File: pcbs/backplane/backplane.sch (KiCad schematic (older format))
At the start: 6 parts, among them P1 CONN_02X04, P2 CONN_02X04, P3 USB_B, P4 CONN_02X09, P5 CONN_02X09, U1 FT232RL

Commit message: Updated electrical spec.
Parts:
- removed P1, P2: CONN_02X04, Pin_Headers:Pin_Header_Straight_2x04, symbol CONN_02X04
- removed P4, P5: CONN_02X09, Pin_Headers:Pin_Header_Straight_2x09, symbol CONN_02X09
- removed U1: FT232RL, Housings_SSOP:SSOP-28_5.3x10.2mm_Pitch0.65mm, symbol FT232RL
- added P1, P2: CONN_02X03, Pin_Headers:Pin_Header_Straight_2x03, symbol CONN_02X03
- added P4, P5: CONN_02X07, Pin_Headers:Pin_Header_Straight_2x07, symbol CONN_02X07
- added U1: CH340G, SMD_Packages:SO-16-N, symbol CH340G
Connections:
- net labels added: 5V, ADC4, GPIO0, UART_RX, nRST
- net labels removed: PWM1, PWM2, SPI_CLK, SPI_CS, SPI_MISO, SPI_MOSI, VCC, Vcc
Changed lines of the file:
@@
 LIBS:silabs
 LIBS:ft232rl
+LIBS:ch340g
 LIBS:backplane-cache
 EELAYER 25 0
@@
 $EndDescr
 $Comp
-L CONN_02X04 P1
-U 1 1 5948E65F
-P 2100 2400
-F 0 "P1" H 2100 2650 50  0000 C CNN
-F 1 "CONN_02X04" H 2100 2150 50  0000 C CNN
-F 2 "Pin_Headers:Pin_Header_Straight_2x04" H 2100 1200 50  0001 C CNN
-F 3 "" H 2100 1200 50  0000 C CNN
-	1    2100 2400
-	1    0    0    -1
-$EndComp
-$Comp
 L USB_B P3
 U 1 1 5948EBA5
@@
 	-1   0    0    1
 $EndComp
-$Comp
-L CONN_02X09 P4
-U 1 1 5948FBD0
-P 7500 2500
-F 0 "P4" H 7500 3000 50  0000 C CNN
-F 1 "CONN_02X09" V 7500 2500 50  0000 C CNN
-F 2 "Pin_Headers:Pin_Header_Straight_2x09" H 7500 1300 50  0001 C CNN
-F 3 "" H 7500 1300 50  0000 C CNN
-	1    7500 2500
-	1    0    0    -1
-$EndComp
 Text GLabel 1850 2250 0    60   UnSpc ~ 0
-Vcc
+5V
 Text GLabel 1850 2350 0    60   UnSpc ~ 0
 ADC1
 Text GLabel 1850 2450 0    60   UnSpc ~ 0
 ADC2
-Text GLabel 1850 2550 0    60   UnSpc ~ 0
+Text GLabel 2350 2350 2    60   UnSpc ~ 0
 ADC3
 Text GLabel 2350 2250 2    60   UnSpc ~ 0
 GND
-Text GLabel 2350 2350 2    60   UnSpc ~ 0
-GND
-Text GLabel 2350 2450 2    60   UnSpc ~ 0
-DAC1
-Text GLabel 2350 2550 2    60   UnSpc ~ 0
-DAC2
-Text GLabel 7250 2100 0    60   UnSpc ~ 0
-VCC
-Text GLabel 7250 2200 0    60   UnSpc ~ 0
-GND
-Text GLabel 7250 2300 0    60   UnSpc ~ 0
-SPI_CLK
-Text GLabel 7250 2400 0    60   UnSpc ~ 0
-SPI_MISO
-Text GLabel 7250 2500 0    60   UnSpc ~ 0
-SPI_MOSI
-Text GLabel 7250 2600 0    60   UnSpc ~ 0
-SPI_CS
-Text GLabel 7250 2700 0    60   UnSpc ~ 0
-I2C_SCL
-Text GLabel 7250 2800 0    60   UnSpc ~ 0
-I2C_SDA
-Text GLabel 7250 2900 0    60   UnSpc ~ 0
-UART_TX
 $Comp
-L FT232RL U1
-U 1 1 59490896
-P 5150 4050
-F 0 "U1" H 4400 5250 60  0000 C CNN
-F 1 "FT232RL" H 5150 4050 60  0000 C CNN
-F 2 "Housings_SSOP:SSOP-28_5.3x10.2mm_Pitch0.65mm" H 5150 4050 60  0001 C CNN
-F 3 "" H 5150 4050 60  0001 C CNN
-	1    5150 4050
+L CONN_02X03 P1
+U 1 1 594F86D2
+P 2100 2350
+F 0 "P1" H 2100 2550 50  0000 C CNN
+F 1 "CONN_02X03" H 2100 2150 50  0001 C CNN
+F 2 "Pin_Headers:Pin_Header_Straight_2x03" H 2100 1150 50  0001 C CNN
+F 3 "" H 2100 1150 50  0000 C CNN
+	1    2100 2350
 	1    0    0    -1
 $EndComp
-Text GLabel 7750 2100 2    60   UnSpc ~ 0
-PWM1
-Text GLabel 7750 2200 2    60   UnSpc ~ 0
-PWM2
-Text GLabel 7750 2300 2    60   UnSpc ~ 0
-DAC1
-Text GLabel 7750 2400 2    60   UnSpc ~ 0
-DAC2
-Text GLabel 7750 2500 2    60   UnSpc ~ 0
-GPIO1
-Text GLabel 7750 2600 2    60   UnSpc ~ 0
-GPIO2
-Text GLabel 7750 2700 2    60   UnSpc ~ 0
-GPIO3
-Text GLabel 7750 2800 2    60   UnSpc ~ 0
-GPIO4
-Text GLabel 7750 2900 2    60   UnSpc ~ 0
-UART_TX
+Text GLabel 2350 2450 2    60   UnSpc ~ 0
+ADC4
 $Comp
-L CONN_02X04 P2
-U 1 1 59490E80
-P 2100 3250
-F 0 "P2" H 2100 3500 50  0000 C CNN
-F 1 "CONN_02X04" H 2100 3000 50  0000 C CNN
-F 2 "Pin_Headers:Pin_Header_Straight_2x04" H 2100 2050 50  0001 C CNN
-F 3 "" H 2100 2050 50  0000 C CNN
-	1    2100 3250
+L CH340G U1
+U 1 1 594FA4BA
+P 5150 4200
+F 0 "U1" H 5150 3700 60  0000 C CNN
+F 1 "CH340G" H 5150 4700 60  0000 C CNN
+F 2 "SMD_Packages:SO-16-N" H 5350 3550 60  0001 C CNN
+F 3 "http://cdn2.boxtec.ch/pub/diverse/ch340g-datasheet.pdf" H 5350 3550 60  0001 C CNN
+	1    5150 4200
 	1    0    0    -1
 $EndComp
-Text GLabel 1850 3100 0    60   UnSpc ~ 0
-Vcc
-Text GLabel 1850 3200 0    60   UnSpc ~ 0
-ADC1
-Text GLabel 1850 3300 0    60   UnSpc ~ 0
-ADC2
-Text GLabel 1850 3400 0    60   UnSpc ~ 0
-ADC3
-Text GLabel 2350 3100 2    60   UnSpc ~ 0
+Text GLabel 9050 2000 0    60   UnSpc ~ 0
+5V
+Text GLabel 9050 2100 0    60   UnSpc ~ 0
 GND
-Text GLabel 2350 3200 2    60   UnSpc ~ 0
-GND
-Text GLabel 2350 3300 2    60   UnSpc ~ 0
+Text GLabel 9050 2200 0    60   UnSpc ~ 0
+I2C_SCL
+Text GLabel 9050 2300 0    60   UnSpc ~ 0
+I2C_SDA
+Text GLabel 9050 2400 0    60   UnSpc ~ 0
+UART_TX
+Text GLabel 9050 2600 0    60   UnSpc ~ 0
 DAC1
-Text GLabel 2350 3400 2    60   UnSpc ~ 0
+Text GLabel 9550 2600 2    60   UnSpc ~ 0
 DAC2
+Text GLabel 9550 2300 2    60   UnSpc ~ 0
+GPIO3
+Text GLabel 9550 2400 2    60   UnSpc ~ 0
+GPIO4
+Text GLabel 9050 2500 0    60   UnSpc ~ 0
+UART_RX
+Text GLabel 9550 2200 2    60   UnSpc ~ 0
+GPIO2
+Text GLabel 9550 2100 2    60   UnSpc ~ 0
+GPIO1
+Text GLabel 9550 2000 2    60   UnSpc ~ 0
+GPIO0
+Text GLabel 9550 2500 2    60   UnSpc ~ 0
+nRST
 $Comp
-L CONN_02X09 P5
-U 1 1 59490EE5
-P 9650 2500
-F 0 "P5" H 9650 3000 50  0000 C CNN
-F 1 "CONN_02X09" V 9650 2500 50  0000 C CNN
-F 2 "Pin_Headers:Pin_Header_Straight_2x09" H 9650 1300 50  0001 C CNN
-F 3 "" H 9650 1300 50  0000 C CNN
-	1    9650 2500
+L CONN_02X07 P4
+U 1 1 594FADC8
+P 9300 2300
+F 0 "P4" H 9300 2700 50  0000 C CNN
+F 1 "CONN_02X07" V 9300 2300 50  0001 C CNN
+F 2 "Pin_Headers:Pin_Header_Straight_2x07" H 9300 1100 50  0001 C CNN
+F 3 "" H 9300 1100 50  0000 C CNN
+	1    9300 2300
 	1    0    0    -1
 $EndComp
-Text GLabel 9400 2100 0    60   UnSpc ~ 0
-VCC
-Text GLabel 9400 2200 0    60   UnSpc ~ 0
+Text GLabel 9050 3000 0    60   UnSpc ~ 0
+5V
+Text GLabel 9050 3100 0    60   UnSpc ~ 0
 GND
-Text GLabel 9400 2300 0    60   UnSpc ~ 0
-SPI_CLK
-Text GLabel 9400 2400 0    60   UnSpc ~ 0
-SPI_MISO
-Text GLabel 9400 2500 0    60   UnSpc ~ 0
-SPI_MOSI
-Text GLabel 9400 2600 0    60   UnSpc ~ 0
-SPI_CS
-Text GLabel 9400 2700 0    60   UnSpc ~ 0
+Text GLabel 9050 3200 0    60   UnSpc ~ 0
 I2C_SCL
-Text GLabel 9400 2800 0    60   UnSpc ~ 0
+Text GLabel 9050 3300 0    60   UnSpc ~ 0
 I2C_SDA
-Text GLabel 9400 2900 0    60   UnSpc ~ 0
+Text GLabel 9050 3400 0    60   UnSpc ~ 0
 UART_TX
-Text GLabel 9900 2100 2    60   UnSpc ~ 0
-PWM1
-Text GLabel 9900 2200 2    60   UnSpc ~ 0
-PWM2
-Text GLabel 9900 2300 2    60   UnSpc ~ 0
+Text GLabel 9050 3600 0    60   UnSpc ~ 0
 DAC1
-Text GLabel 9900 2400 2    60   UnSpc ~ 0
+Text GLabel 9550 3600 2    60   UnSpc ~ 0
 DAC2
-Text GLabel 9900 2500 2    60   UnSpc ~ 0
+Text GLabel 9550 3300 2    60   UnSpc ~ 0
+GPIO3
+Text GLabel 9550 3400 2    60   UnSpc ~ 0
+GPIO4
+Text GLabel 9050 3500 0    60   UnSpc ~ 0
+UART_RX
+Text GLabel 9550 3200 2    60   UnSpc ~ 0
+GPIO2
+Text GLabel 9550 3100 2    60   UnSpc ~ 0
 GPIO1
-Text GLabel 9900 2600 2    60   UnSpc ~ 0
-GPIO2
-Text GLabel 9900 2700 2    60   UnSpc ~ 0
-GPIO3
-Text GLabel 9900 2800 2    60   UnSpc ~ 0
-GPIO4
-Text GLabel 9900 2900 2    60   UnSpc ~ 0
-UART_TX
+Text GLabel 9550 3000 2    60   UnSpc ~ 0
+GPIO0
+Text GLabel 9550 3500 2    60   UnSpc ~ 0
+nRST
+$Comp
+L CONN_02X07 P5
+U 1 1 594FAEEA
+P 9300 3300
+F 0 "P5" H 9300 3700 50  0000 C CNN
+F 1 "CONN_02X07" V 9300 3300 50  0001 C CNN
+F 2 "Pin_Headers:Pin_Header_Straight_2x07" H 9300 2100 50  0001 C CNN
+F 3 "" H 9300 2100 50  0000 C CNN
+	1    9300 3300
+	1    0    0    -1
+$EndComp
+Text GLabel 1850 2900 0    60   UnSpc ~ 0
+5V
+Text GLabel 1850 3000 0    60   UnSpc ~ 0
+ADC1
+Text GLabel 1850 3100 0    60   UnSpc ~ 0
+ADC2
+Text GLabel 2350 3000 2    60   UnSpc ~ 0
+ADC3
+Text GLabel 2350 2900 2    60   UnSpc ~ 0
+GND
+$Comp
+L CONN_02X03 P2
+U 1 1 594FAFF9
+P 2100 3000
+F 0 "P2" H 2100 3200 50  0000 C CNN
+F 1 "CONN_02X03" H 2100 2800 50  0001 C CNN
+F 2 "Pin_Headers:Pin_Header_Straight_2x03" H 2100 1800 50  0001 C CNN
+F 3 "" H 2100 1800 50  0000 C CNN
+	1    2100 3000
+	1    0    0    -1
+$EndComp
+Text GLabel 2350 3100 2    60   UnSpc ~ 0
+ADC4
 $EndSCHEMATC

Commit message: Changed electrical spec again.
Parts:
- added C? (x2): 22p, Resistors_SMD:R_0805, symbol C
- added Q? (x2): MMBT3904, SOT-23, symbol MMBT3904
- added R? (x2): 10k, Resistors_SMD:R_0805, symbol R
- added U?: LM2840, symbol LM2840
- added Y?: Crystal, Crystals:Crystal_HC49-SD_SMD, symbol Crystal
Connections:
- net labels added: +5V, 3.3V, A5V, AGND, D+, D-, DTR, RTS
- net labels removed: 5V
- wire segments 0 -> 34
- no-connect marks 0 -> 5
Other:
- moved on the sheet: P3

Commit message: Schematics of backplane done.
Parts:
- removed U?: LM2840, symbol LM2840
- added C1: 10u, Resistors_SMD:R_0805, symbol C
- added C2, C4, C8: 1u, Resistors_SMD:R_0805, symbol C
- added C3, C5, C9: 100n, Resistors_SMD:R_0805, symbol C
- added D1, D2, D3, D4, D5, D6: LED, LEDs:LED_0805, symbol LED
- added P2: CONN_01X10, Samtec Connectors:Samtec-PHT-1-9-01-L-S, symbol CONN_01X10
- added P7, P8: CONN_01X03, Samtec Connectors:Samtec-PHT-1-3-01-L-S, symbol CONN_01X03
- added R1, R2, R3, R4, R7, R8: 1k, Resistors_SMD:R_0805, symbol R
- added U1, U3: LM358, SMD_Packages:SOIC-8-N, symbol LM358
- added U2: TC1262-33VDB, SOT-223, symbol TC1262-33VDB
- gave numbers to parts that had none: 7
- renumbered P3 to P1, P1 to P3, P2 to P4, P4 to P5, P5 to P6, U1 to U4
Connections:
- net labels added: +3.3V, 5V, LED_3.3V, LED_5V
- net labels removed: A5V, AGND
- wire segments 34 -> 110
- no-connect marks 5 -> 8
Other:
- note added: "ATTENTION: RX_CH340G has to be connected to TX_ESP8266. The same goes for\nTX_CH340G and RX_EXP8266. \n"
- note added: "Auto program circuit, which is needed by the esptool to program via USB."
- note added: "Brings up to 500mA output.\nOptionally this IC can be substituted by the TS2940, which can provide up to 1A."
- note added: "Jumper enables possibility to turn off all LEDs."
- note added: "Make debugging easier."
- note added: "Place decoupling capacitors close to component."
- note added: "Starts blinking when transmission is ongoing, else const. on."
- moved on the sheet: C6, C7, P1, P3, P4, P5, P6, Q1, Q2, R5, R6, U4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

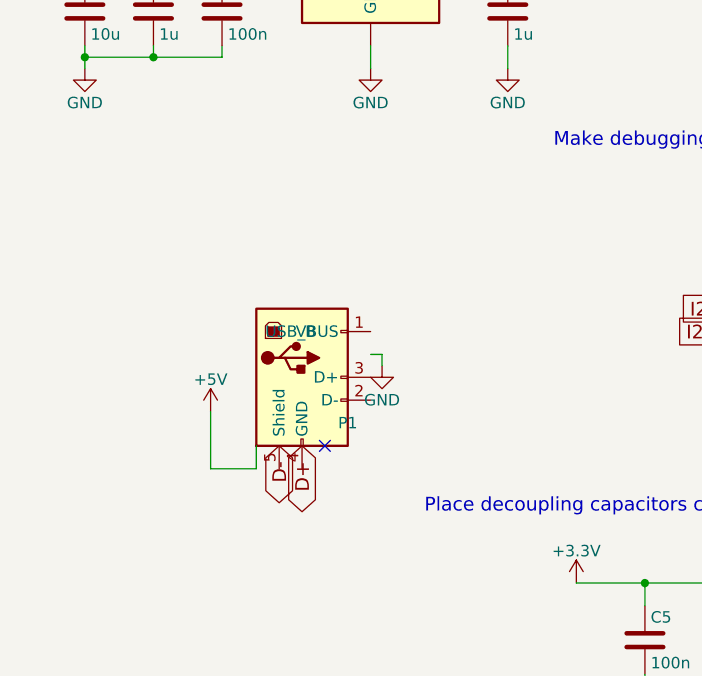
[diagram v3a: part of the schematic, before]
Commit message: Came quite far with backplane design. Not finished yet.
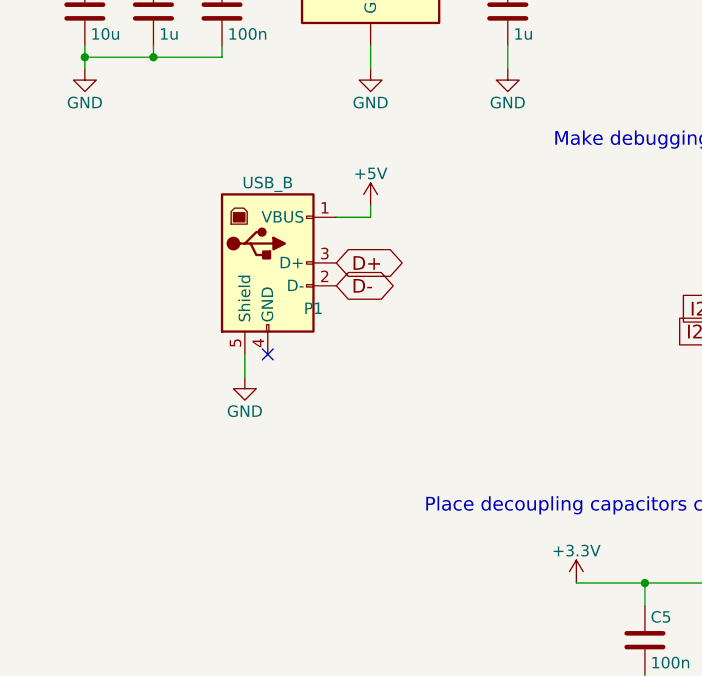
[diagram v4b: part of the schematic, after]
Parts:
- P1: footprint MyUSB:USB3145-30-1-A -> myUSB:ZX62D-B-5P8(30); Farnell 2443141 -> 2554980
- P2: footprint Samtec Connectors:Samtec-PHT-1-9-01-L-S -> mySamtec:Samtec-PHT-1-9-01-L-S
- P7, P8: footprint Samtec Connectors:Samtec-PHT-1-3-01-L-S -> mySamtec:Samtec-PHT-1-3-01-L-S
- Y1: footprint Crystals:Crystal_HC49-SD_SMD -> Crystals:Crystal_SMD_HC49-SD
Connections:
- net +5V: now also P1.1 (VBUS)
- net D+: now also P1.3 (D+)
- net D-: now also P1.2 (D-)
- net GND: now also P1.5 (Shield)
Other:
- moved on the sheet: P1
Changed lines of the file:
@@
 L USB_B P1
 U 1 1 5948EBA5
-P 1850 3000
-F 0 "P1" H 2050 2800 50  0000 C CNN
-F 1 "USB_B" H 1800 3200 50  0000 C CNN
-F 2 "MyUSB:USB3145-30-1-A" V 1800 2900 50  0001 C CNN
-F 3 "http://www.farnell.com/datasheets/1841848.pdf" V 1800 2900 50  0001 C CNN
-F 4 "2443141" H 1850 3000 60  0001 C CNN "Farnell"
-	1    1850 3000
+P 1700 2500
+F 0 "P1" H 1900 2300 50  0000 C CNN
+F 1 "USB_B" H 1700 2850 50  0000 C CNN
+F 2 "myUSB:ZX62D-B-5P8(30)" V 1650 2400 50  0001 C CNN
+F 3 "http://www.farnell.com/cad/2110767.pdf" V 1650 2400 50  0001 C CNN
+F 4 "2554980" H 1700 2500 60  0001 C CNN "Farnell"
+	1    1700 2500
 	1    0    0    -1
 $EndComp
@@
 F 0 "Y1" H 4150 4600 50  0000 C CNN
 F 1 "Crystal" H 4150 4300 50  0000 C CNN
-F 2 "Crystals:Crystal_HC49-SD_SMD" H 4150 4450 50  0001 C CNN
+F 2 "Crystals:Crystal_SMD_HC49-SD" H 4150 4450 50  0001 C CNN
 F 3 "http://www.farnell.com/datasheets/1658661.pdf" H 4150 4450 50  0001 C CNN
 F 4 "9713344" H 4150 4450 60  0001 C CNN "Farnell"
@@
 	1    0    0    -1
 $EndComp
-Text GLabel 1850 3300 3    60   BiDi ~ 0
+Text GLabel 2000 2500 2    60   BiDi ~ 0
 D+
-Text GLabel 1750 3300 3    60   BiDi ~ 0
+Text GLabel 2000 2600 2    60   BiDi ~ 0
 D-
 Text GLabel 5300 4100 0    60   BiDi ~ 0
@@
 L +5V #PWR03
 U 1 1 594FDB60
-P 1450 3150
-F 0 "#PWR03" H 1450 3000 50  0001 C CNN
-F 1 "+5V" H 1450 3290 50  0000 C CNN
-F 2 "" H 1450 3150 50  0000 C CNN
-F 3 "" H 1450 3150 50  0000 C CNN
-	1    1450 3150
+P 2150 2250
+F 0 "#PWR03" H 2150 2100 50  0001 C CNN
+F 1 "+5V" H 2150 2390 50  0000 C CNN
+F 2 "" H 2150 2250 50  0000 C CNN
+F 3 "" H 2150 2250 50  0000 C CNN
+	1    2150 2250
 	1    0    0    -1
 $EndComp
@@
 L GND #PWR04
 U 1 1 594FE150
-P 2200 2950
-F 0 "#PWR04" H 2200 2700 50  0001 C CNN
-F 1 "GND" H 2200 2800 50  0000 C CNN
-F 2 "" H 2200 2950 50  0000 C CNN
-F 3 "" H 2200 2950 50  0000 C CNN
-	1    2200 2950
+P 1600 3000
+F 0 "#PWR04" H 1600 2750 50  0001 C CNN
+F 1 "GND" H 1600 2850 50  0000 C CNN
+F 2 "" H 1600 3000 50  0000 C CNN
+F 3 "" H 1600 3000 50  0000 C CNN
+	1    1600 3000
 	1    0    0    -1
 $EndComp
@@
 	3850 4800 3850 4850
 Wire Wire Line
-	1650 3300 1650 3400
-Wire Wire Line
-	1650 3400 1450 3400
-Wire Wire Line
-	1450 3400 1450 3150
-Wire Wire Line
 	9750 2050 9900 2050
 Wire Wire Line
@@
 F 0 "P8" H 9250 5950 50  0000 C CNN
 F 1 "CONN_01X03" V 9350 5750 50  0000 C CNN
-F 2 "Samtec Connectors:Samtec-PHT-1-3-01-L-S" H 9250 5750 50  0001 C CNN
+F 2 "mySamtec:Samtec-PHT-1-3-01-L-S" H 9250 5750 50  0001 C CNN
 F 3 "http://suddendocs.samtec.com/catalog_english/pht.pdf" H 9250 5750 50  0001 C CNN
 	1    9250 5750
@@
 F 0 "P2" H 4100 3200 50  0000 C CNN
 F 1 "CONN_01X10" V 4200 2650 50  0000 C CNN
-F 2 "Samtec Connectors:Samtec-PHT-1-9-01-L-S" H 4100 2650 50  0001 C CNN
+F 2 "mySamtec:Samtec-PHT-1-9-01-L-S" H 4100 2650 50  0001 C CNN
 F 3 "http://suddendocs.samtec.com/catalog_english/pht.pdf" H 4100 2650 50  0001 C CNN
 	1    4100 2650
@@
 Text GLabel 4000 6950 0    60   UnSpc ~ 0
 I2C_SDA
-Wire Wire Line
-	2150 2900 2200 2900
-Wire Wire Line
-	2200 2900 2200 2950
-NoConn ~ 1950 3300
 Text GLabel 5450 5900 3    60   Input ~ 0
 LED_5V
@@
 F 0 "P7" H 9250 4850 50  0000 C CNN
 F 1 "CONN_01X03" V 9350 4650 50  0000 C CNN
-F 2 "Samtec Connectors:Samtec-PHT-1-3-01-L-S" H 9250 4650 50  0001 C CNN
+F 2 "mySamtec:Samtec-PHT-1-3-01-L-S" H 9250 4650 50  0001 C CNN
 F 3 "http://suddendocs.samtec.com/catalog_english/pht.pdf" H 9250 4650 50  0001 C CNN
 	1    9250 4650
@@
 	6500 1150 6500 1200
 Connection ~ 6500 1200
+Wire Wire Line
+	1600 2900 1600 3000
+Wire Wire Line
+	2000 2300 2150 2300
+Wire Wire Line
+	2150 2300 2150 2250
+NoConn ~ 1700 2900
 $EndSCHEMATC

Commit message: Backplane version 1 ready.
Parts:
- removed P2: CONN_01X10, mySamtec:Samtec-PHT-1-9-01-L-S, symbol CONN_01X10
- added 3V3, 5V0, ADC1, ADC2, ADC3, ADC4, DAC1, DAC2, SCL1, SDA1: TEST, myTestPoints:TP_SMD_quadr_1mm, symbol TEST
- added GND1: TEST, myTestPoints:TP_SMD_quadr_3mm, symbol TEST
- added Q3: Si2323, TO_SOT_Packages_SMD:SOT-23, symbol Q_PMOS_GSD
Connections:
- net +3V3: now also 3V3.1
- net +5V: now also 5V0.1, Q3.2 (S); no longer P1.1 (VBUS)
- net ADC1: now also ADC1.1
- net ADC2: now also ADC2.1
- net ADC3: now also ADC3.1
- net ADC4: now also ADC4.1
- net DAC1: now also DAC1.1
- net DAC2: now also DAC2.1
- net GND: now also GND1.1, Q3.1 (G)
- net GPIO0: no longer P6.2 (P2)
- net I2C_SCL: now also SCL1.1
- net I2C_SDA: now also SDA1.1
- net LED_5V: now also D1.2 (A), D2.2 (A), D3.2 (A), D4.2 (A); no longer D1.1 (K), D2.1 (K), D3.1 (K), D4.1 (K)
- net UART_RX: now also U4.3 (RXD); no longer P6.11 (P11), U4.2 (TXD)
- net UART_TX: now also U4.2 (TXD); no longer P6.9 (P9), U4.3 (RXD)
- net nRST: no longer P6.12 (P12)
- net at R2.1: now also D2.1 (K); no longer D2.2 (A)
- net at R1.1: now also D1.1 (K); no longer D1.2 (A)
- net at R4.1: now also D4.1 (K); no longer D4.2 (A)
- net at R3.1: now also D3.1 (K); no longer D3.2 (A)
- new net: P1.1 (VBUS), Q3.3 (D)
- no-connect marks 8 -> 12
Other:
- note added: "Reverse polarization protection."
- moved on the sheet: D1, D2, D3, D4

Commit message: Finished schematics of the analog_board_v0.2 today.
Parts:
- C1: Farnell 2496998 -> 1833812
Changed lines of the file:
@@
 F 2 "Resistors_SMD:R_0805" H 938 1250 50  0001 C CNN
 F 3 "" H 900 1400 50  0000 C CNN
-F 4 "2496998" H 900 1400 60  0001 C CNN "Farnell"
+F 4 "1833812" H 900 1400 60  0001 C CNN "Farnell"
 	1    900  1400
 	1    0    0    -1
